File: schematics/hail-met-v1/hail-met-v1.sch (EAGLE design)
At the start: 99 parts, among them IC1 MCP73871, J1 AVR_SPI_PRG_6PTH, U1 ATMEGA328P, Y1 16MHZ

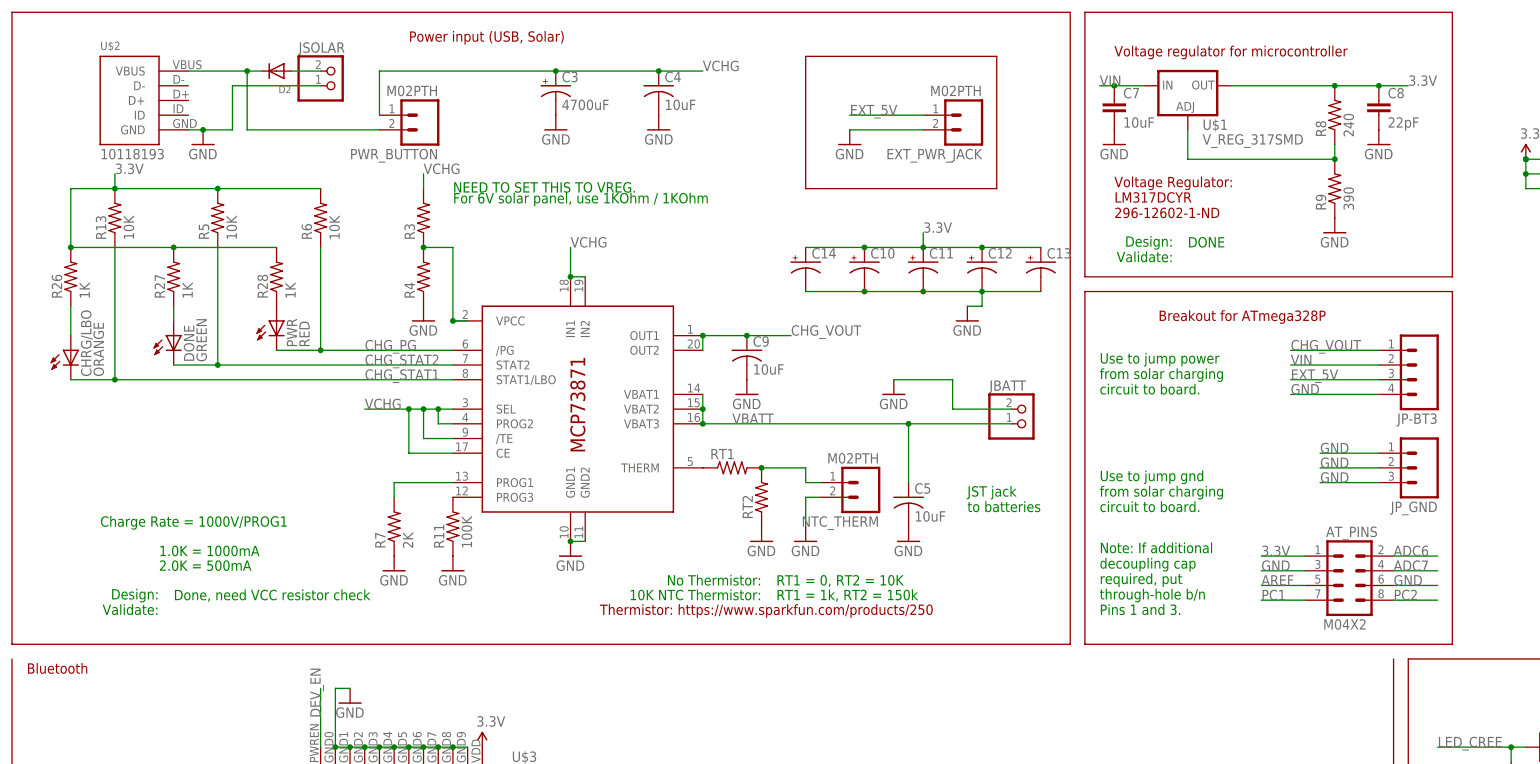
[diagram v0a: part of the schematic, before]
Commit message: updated schematics (v0, v1) and datasheets
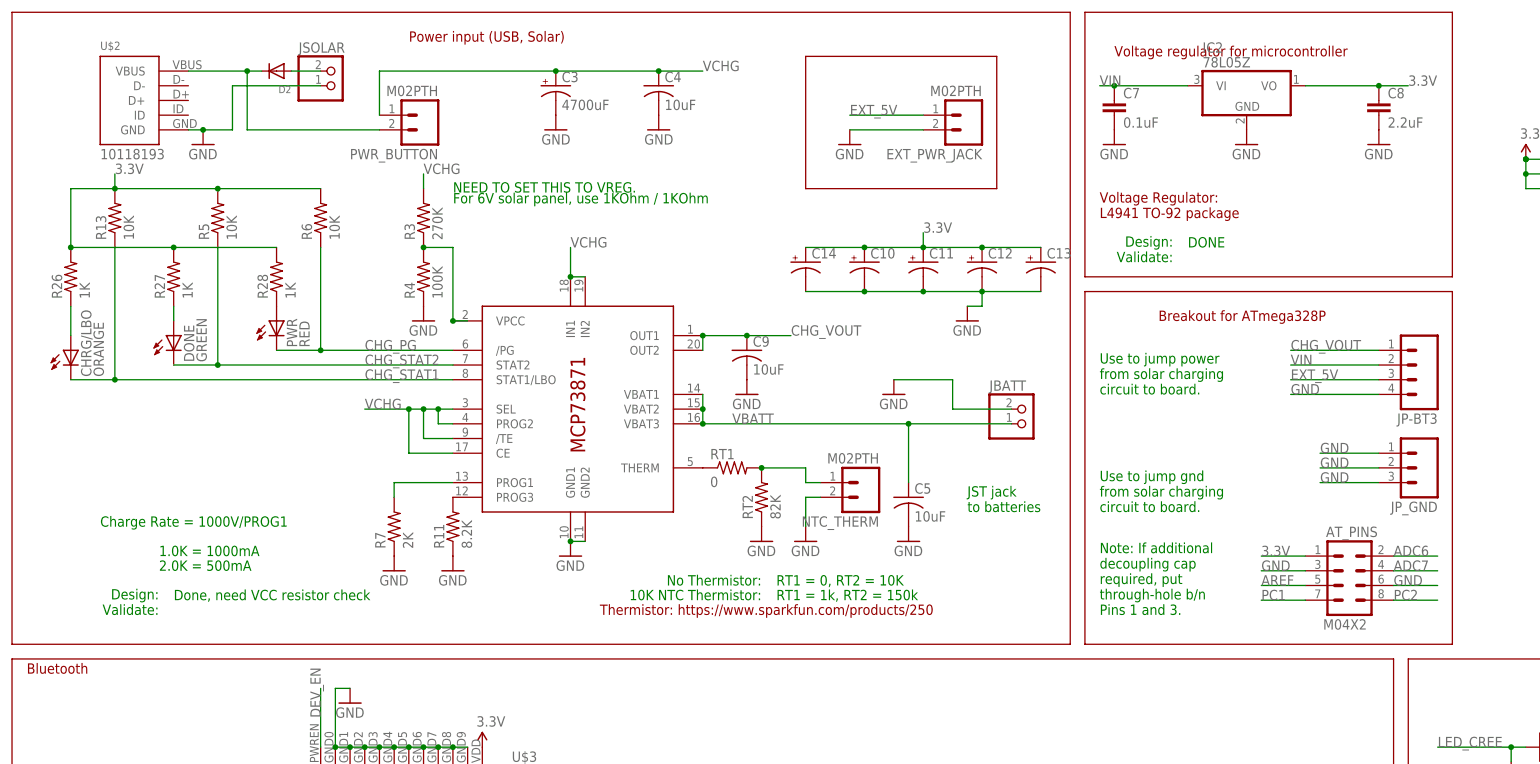
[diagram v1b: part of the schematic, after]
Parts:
- removed R8: 240, SparkFun-Passives:RESISTOR0805-RES
- removed R9: 390, SparkFun-Passives:RESISTOR0805-RES
- removed U$1: V_REG_317SMD, SparkFun:V_REG_317SMD
- added IC2: 78L05Z, adafruit:78L05Z
- C7: value 10uF -> 0.1uF
- C8: value 22pF -> 2.2uF
- R11: value 100K -> 8.2K
- R3: value (none) -> 270K
- R4: value (none) -> 100K
- RT1: value (none) -> 0
- RT2: value (none) -> 82K
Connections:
- removed net N$4: R8.1, R9.2, U$1.ADJ
- net 3.3V: now also IC2.VO; no longer R8.2, U$1.OUT
- net GND: now also IC2.GND; no longer R9.1
- net VIN: now also IC2.VI; no longer U$1.IN
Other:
- note added: "Voltage Regulator: L4941 TO-92 package"
- note removed: "Voltage Regulator: LM317DCYR 296-12602-1-ND"
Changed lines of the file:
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@@
 <part name="P+1" library="SparkFun" deviceset="3.3V" device=""/>
 <part name="GND1" library="SparkFun" deviceset="GND" device=""/>
-<part name="U$1" library="SparkFun" deviceset="V_REG_317" device="SMD"/>
 <part name="GND2" library="SparkFun" deviceset="GND" device=""/>
 <part name="GND3" library="SparkFun" deviceset="GND" device=""/>
@@
 <part name="R5" library="SparkFun-Passives" deviceset="RESISTOR" device="0805-RES" value="10K"/>
 <part name="R6" library="SparkFun-Passives" deviceset="RESISTOR" device="0805-RES" value="10K"/>
-<part name="R3" library="SparkFun-Passives" deviceset="RESISTOR" device="0805-RES"/>
-<part name="R4" library="SparkFun-Passives" deviceset="RESISTOR" device="0805-RES"/>
+<part name="R3" library="SparkFun-Passives" deviceset="RESISTOR" device="0805-RES" value="270K"/>
+<part name="R4" library="SparkFun-Passives" deviceset="RESISTOR" device="0805-RES" value="100K"/>
 <part name="R7" library="SparkFun-Passives" deviceset="RESISTOR" device="0805-RES" value="2K"/>
-<part name="R11" library="SparkFun-Passives" deviceset="RESISTOR" device="0805-RES" value="100K"/>
-<part name="RT1" library="SparkFun-Passives" deviceset="RESISTOR" device="0805-RES"/>
-<part name="RT2" library="SparkFun-Passives" deviceset="RESISTOR" device="0805-RES"/>
-<part name="C7" library="SparkFun-Passives" deviceset="CAP" device="0805" value="10uF"/>
-<part name="C8" library="SparkFun-Passives" deviceset="CAP" device="0805" value="22pF"/>
-<part name="R8" library="SparkFun-Passives" deviceset="RESISTOR" device="0805-RES" value="240"/>
-<part name="R9" library="SparkFun-Passives" deviceset="RESISTOR" device="0805-RES" value="390"/>
+<part name="R11" library="SparkFun-Passives" deviceset="RESISTOR" device="0805-RES" value="8.2K"/>
+<part name="RT1" library="SparkFun-Passives" deviceset="RESISTOR" device="0805-RES" value="0"/>
+<part name="RT2" library="SparkFun-Passives" deviceset="RESISTOR" device="0805-RES" value="82K"/>
+<part name="C7" library="SparkFun-Passives" deviceset="CAP" device="0805" value="0.1uF"/>
+<part name="C8" library="SparkFun-Passives" deviceset="CAP" device="0805" value="2.2uF"/>
 <part name="C1" library="SparkFun-Passives" deviceset="CAP" device="0805" value="0.1uF"/>
 <part name="R1" library="SparkFun-Passives" deviceset="RESISTOR" device="0805-RES"/>
@@
 <part name="GND42" library="SparkFun" deviceset="GND" device=""/>
 <part name="Q1" library="SparkFun" deviceset="TRANSISTOR_NPN" device="SOT23-3"/>
+<part name="IC2" library="adafruit" deviceset="78*" device="Z" technology="L05"/>
 </parts>
 <sheets>
@@
 <wire x1="-17.78" y1="73.66" x2="-50.8" y2="73.66" width="0.1524" layer="94"/>
 <wire x1="-50.8" y1="73.66" x2="-50.8" y2="96.52" width="0.1524" layer="94"/>
-<text x="2.54" y="68.58" size="1.778" layer="94">Voltage Regulator:
-LM317DCYR
-296-12602-1-ND</text>
 <text x="-86.36" y="-96.52" size="1.778" layer="94">Mic required to have dBV
 between -40 and -60</text>
@@
 from solar charging
 circuit to board.</text>
+<wire x1="-187.96" y1="-7.62" x2="50.8" y2="-7.62" width="0.1524" layer="94"/>
+<text x="0" y="68.58" size="1.778" layer="94">Voltage Regulator:
+L4941 TO-92 package
+</text>
 </plain>
 <instances>
@@
 <instance part="P+1" gate="G$1" x="73.66" y="78.74"/>
 <instance part="GND1" gate="1" x="81.28" y="25.4"/>
-<instance part="U$1" gate="G$1" x="15.24" y="91.44"/>
-<instance part="GND2" gate="1" x="40.64" y="66.04"/>
+<instance part="GND2" gate="1" x="25.4" y="81.28"/>
 <instance part="GND3" gate="1" x="48.26" y="81.28"/>
 <instance part="GND4" gate="1" x="2.54" y="81.28"/>
@@
 <instance part="C7" gate="G$1" x="2.54" y="86.36"/>
 <instance part="C8" gate="G$1" x="48.26" y="86.36"/>
-<instance part="R8" gate="G$1" x="40.64" y="86.36" rot="R90"/>
-<instance part="R9" gate="G$1" x="40.64" y="73.66" rot="R90"/>
 <instance part="C1" gate="G$1" x="83.82" y="88.9" rot="R180"/>
 <instance part="R1" gate="G$1" x="66.04" y="-63.5" rot="R180"/>
@@
 <instance part="GND42" gate="1" x="-22.86" y="50.8"/>
 <instance part="Q1" gate="G$1" x="76.2" y="-22.86"/>
+<instance part="IC2" gate="A1" x="25.4" y="91.44"/>
 </instances>
 <busses>
@@
 <pinref part="GND13" gate="1" pin="GND"/>
 <pinref part="RT2" gate="G$1" pin="1"/>
-</segment>
-<segment>
-<pinref part="GND2" gate="1" pin="GND"/>
-<pinref part="R9" gate="G$1" pin="1"/>
 </segment>
 <segment>
@@
 <pinref part="GND20" gate="1" pin="GND"/>
 </segment>
+<segment>
+<pinref part="IC2" gate="A1" pin="GND"/>
+<pinref part="GND2" gate="1" pin="GND"/>
+</segment>
 </net>
 <net name="VIN" class="0">
@@
 </segment>
 <segment>
-<pinref part="U$1" gate="G$1" pin="IN"/>
 <label x="0" y="91.44" size="1.778" layer="95"/>
 <pinref part="C7" gate="G$1" pin="1"/>
-<wire x1="2.54" y1="91.44" x2="7.62" y2="91.44" width="0.1524" layer="91"/>
 <wire x1="0" y1="91.44" x2="2.54" y2="91.44" width="0.1524" layer="91"/>
 <junction x="2.54" y="91.44"/>
-</segment>
-</net>
-<net name="N$4" class="0">
-<segment>
-<pinref part="U$1" gate="G$1" pin="ADJ"/>
-<wire x1="15.24" y1="83.82" x2="15.24" y2="78.74" width="0.1524" layer="91"/>
-<wire x1="15.24" y1="78.74" x2="40.64" y2="78.74" width="0.1524" layer="91"/>
-<wire x1="40.64" y1="78.74" x2="40.64" y2="81.28" width="0.1524" layer="91"/>
-<pinref part="R9" gate="G$1" pin="2"/>
-<junction x="40.64" y="78.74"/>
-<pinref part="R8" gate="G$1" pin="1"/>
+<pinref part="IC2" gate="A1" pin="VI"/>
+<wire x1="2.54" y1="91.44" x2="15.24" y2="91.44" width="0.1524" layer="91"/>
 </segment>
 </net>
 <net name="3.3V" class="0">
 <segment>
-<pinref part="U$1" gate="G$1" pin="OUT"/>
-<wire x1="40.64" y1="91.44" x2="22.86" y2="91.44" width="0.1524" layer="91"/>
+<wire x1="48.26" y1="91.44" x2="35.56" y2="91.44" width="0.1524" layer="91"/>
 <wire x1="53.34" y1="91.44" x2="48.26" y2="91.44" width="0.1524" layer="91"/>
 <label x="53.34" y="91.44" size="1.778" layer="95"/>
-<pinref part="R8" gate="G$1" pin="2"/>
-<junction x="40.64" y="91.44"/>
 <pinref part="C8" gate="G$1" pin="1"/>
-<wire x1="48.26" y1="91.44" x2="40.64" y2="91.44" width="0.1524" layer="91"/>
 <junction x="48.26" y="91.44"/>
-</segment>
-<segment>
+<pinref part="IC2" gate="A1" pin="VO"/>
+</segment>
+<segment>

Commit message: updated schematic with charge termination current resistor
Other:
- note added: "PROG3 - Charging termination current: 125mA: 8.2K (our spec) 1mA: 100K (Adafruit spec)"
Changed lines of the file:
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@@
 <text x="-55.88" y="5.08" size="1.778" layer="91" distance="5">RT1 = 0, RT2 = 10K</text>
 <text x="-55.88" y="2.54" size="1.778" layer="91" distance="5">RT1 = 1k, RT2 = 150k</text>
-<text x="-172.72" y="15.24" size="1.778" layer="91" distance="5">Charge Rate = 1000V/PROG1</text>
-<text x="-162.56" y="10.16" size="1.778" layer="91" distance="5">1.0K = 1000mA</text>
-<text x="-162.56" y="7.62" size="1.778" layer="91" distance="5">2.0K = 500mA</text>
+<text x="-180.34" y="17.78" size="1.778" layer="91" distance="5">Charge Rate = 1000V/PROG1</text>
+<text x="-170.18" y="12.7" size="1.778" layer="91" distance="5">1.0K = 1000mA</text>
+<text x="-170.18" y="10.16" size="1.778" layer="91" distance="5">2.0K = 500mA</text>
 <text x="-111.76" y="71.12" size="1.778" layer="91" distance="5">NEED TO SET THIS TO VREG.
 For 6V solar panel, use 1KOhm / 1KOhm</text>
@@
 <text x="12.7" y="60.96" size="1.778" layer="91" align="bottom-right">Design:
 Validate:</text>
-<text x="-162.56" y="0" size="1.778" layer="91" align="bottom-right">Design:
+<text x="-167.64" y="0" size="1.778" layer="91" align="bottom-right">Design:
 Validate:</text>
 <text x="68.58" y="-96.52" size="1.778" layer="91" align="bottom-right">Design:
@@
 <wire x1="220.98" y1="-106.68" x2="53.34" y2="-106.68" width="0.1524" layer="94"/>
 <wire x1="53.34" y1="-106.68" x2="53.34" y2="-7.62" width="0.1524" layer="94"/>
-<text x="-160.02" y="2.54" size="1.778" layer="91">Done, need VCC resistor check</text>
+<text x="-165.1" y="2.54" size="1.778" layer="91">Done, need VCC resistor check</text>
 <wire x1="50.8" y1="-7.62" x2="50.8" y2="-106.68" width="0.1524" layer="94"/>
 <wire x1="50.8" y1="-106.68" x2="-187.96" y2="-106.68" width="0.1524" layer="94"/>
@@
 L4941 TO-92 package
 </text>
+<text x="-180.34" y="25.4" size="1.778" layer="91">PROG3 - Charging termination current:
+  125mA: 8.2K (our spec)
+  1mA: 100K (Adafruit spec)</text>
 </plain>
 <instances>

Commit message: updated board v1
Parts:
- removed MIC_R: (no value), adafruit:JST_2PIN-SMT
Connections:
- removed net MIC_R+: MIC_R.2, U$3.MIC_R+
- removed net MIC_R-: MIC_R.1, U$3.MIC_R-
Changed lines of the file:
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@@
 <part name="JSOLAR" library="adafruit" deviceset="JST_2PIN" device="-SMT"/>
 <part name="MIC_L" library="adafruit" deviceset="JST_2PIN" device="-SMT"/>
-<part name="MIC_R" library="adafruit" deviceset="JST_2PIN" device="-SMT"/>
 <part name="SPK_L" library="adafruit" deviceset="JST_2PIN" device="-SMT"/>
 <part name="SPK_R" library="adafruit" deviceset="JST_2PIN" device="-SMT"/>
@@
 <instance part="JSOLAR" gate="G$1" x="-132.08" y="91.44"/>
 <instance part="MIC_L" gate="G$1" x="-53.34" y="-66.04"/>
-<instance part="MIC_R" gate="G$1" x="-53.34" y="-83.82"/>
 <instance part="SPK_L" gate="G$1" x="-43.18" y="-43.18"/>
 <instance part="SPK_R" gate="G$1" x="-43.18" y="-53.34"/>
@@
 </segment>
 </net>
-<net name="MIC_R-" class="0">
-<segment>
-<pinref part="U$3" gate="G$1" pin="MIC_R-"/>
-<wire x1="-86.36" y1="-58.42" x2="-76.2" y2="-58.42" width="0.1524" layer="91"/>
-<wire x1="-76.2" y1="-81.28" x2="-76.2" y2="-58.42" width="0.1524" layer="91"/>
-<pinref part="MIC_R" gate="G$1" pin="1"/>
-<wire x1="-55.88" y1="-81.28" x2="-76.2" y2="-81.28" width="0.1524" layer="91"/>
-<label x="-71.12" y="-81.28" size="1.778" layer="95"/>
-</segment>
-</net>
 <net name="MIC_L-" class="0">
 <segment>
@@
 </segment>
 </net>
-<net name="MIC_R+" class="0">
-<segment>
-<pinref part="U$3" gate="G$1" pin="MIC_R+"/>
-<wire x1="-86.36" y1="-63.5" x2="-73.66" y2="-63.5" width="0.1524" layer="91"/>
-<wire x1="-73.66" y1="-83.82" x2="-73.66" y2="-63.5" width="0.1524" layer="91"/>
-<pinref part="MIC_R" gate="G$1" pin="2"/>
-<wire x1="-73.66" y1="-83.82" x2="-55.88" y2="-83.82" width="0.1524" layer="91"/>
-<label x="-71.12" y="-83.82" size="1.778" layer="95"/>
-</segment>
-</net>
